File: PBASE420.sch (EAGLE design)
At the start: 13 parts, among them J1 DC_2_1MM, SW1 MK-12C02-PB

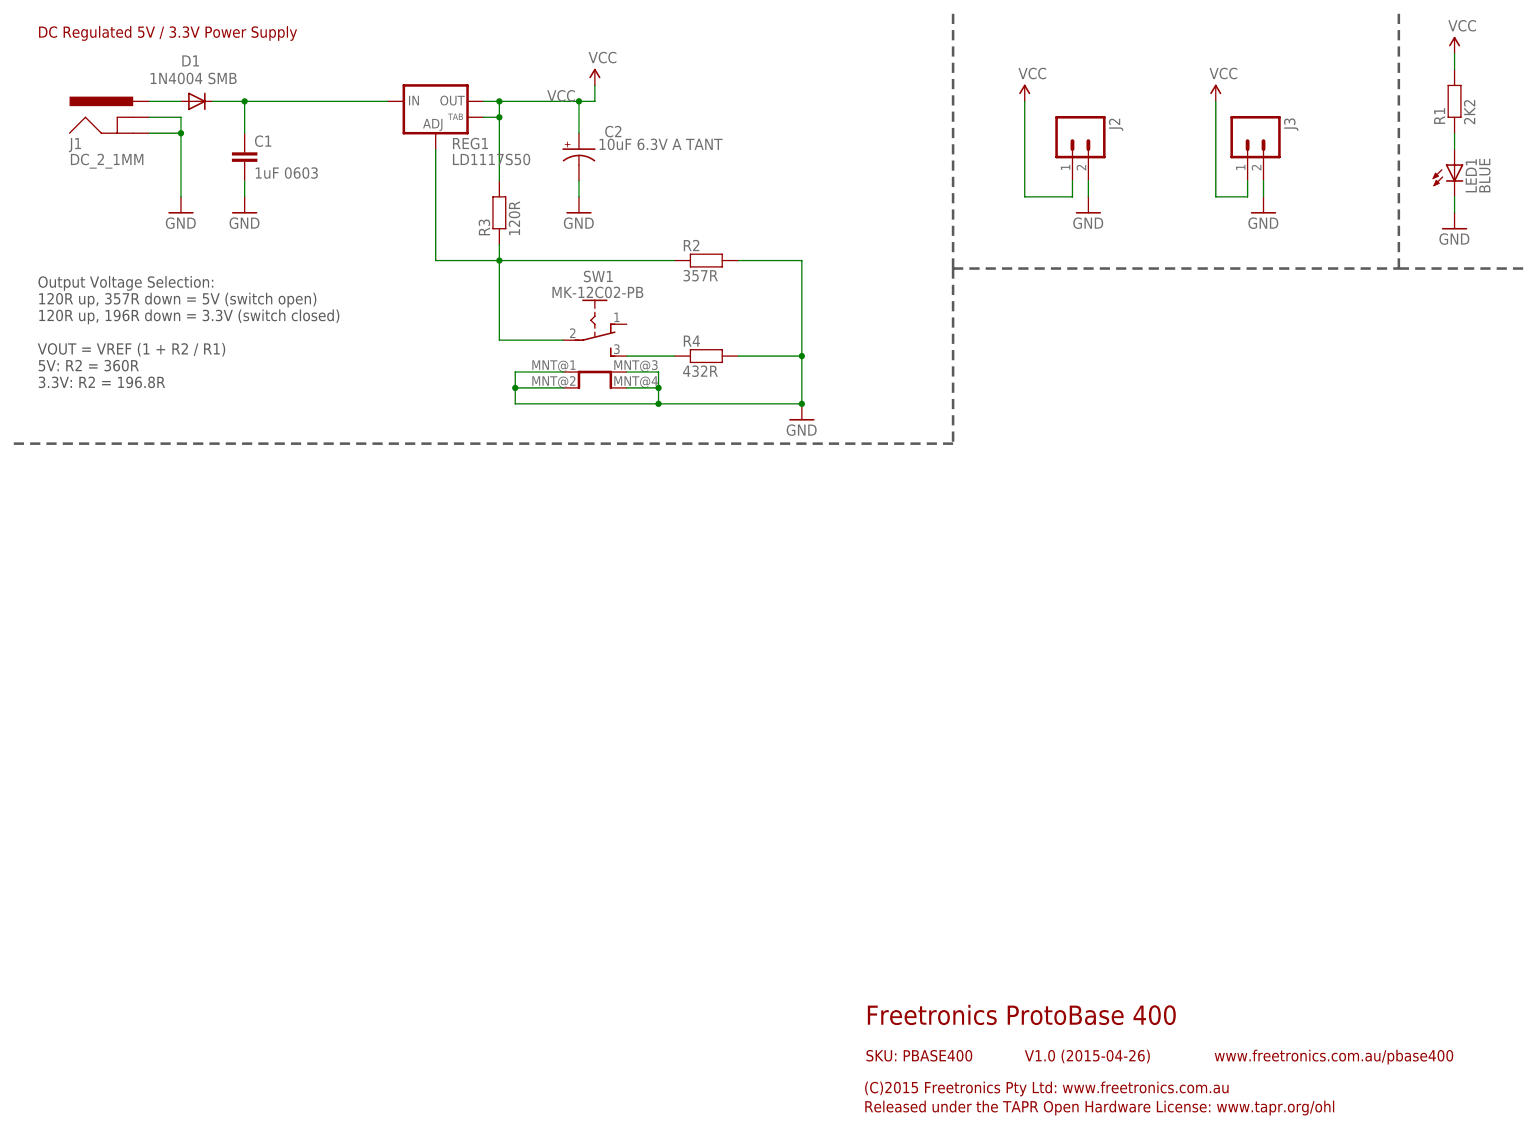
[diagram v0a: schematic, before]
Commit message: Updated silkscreen, designators, and README
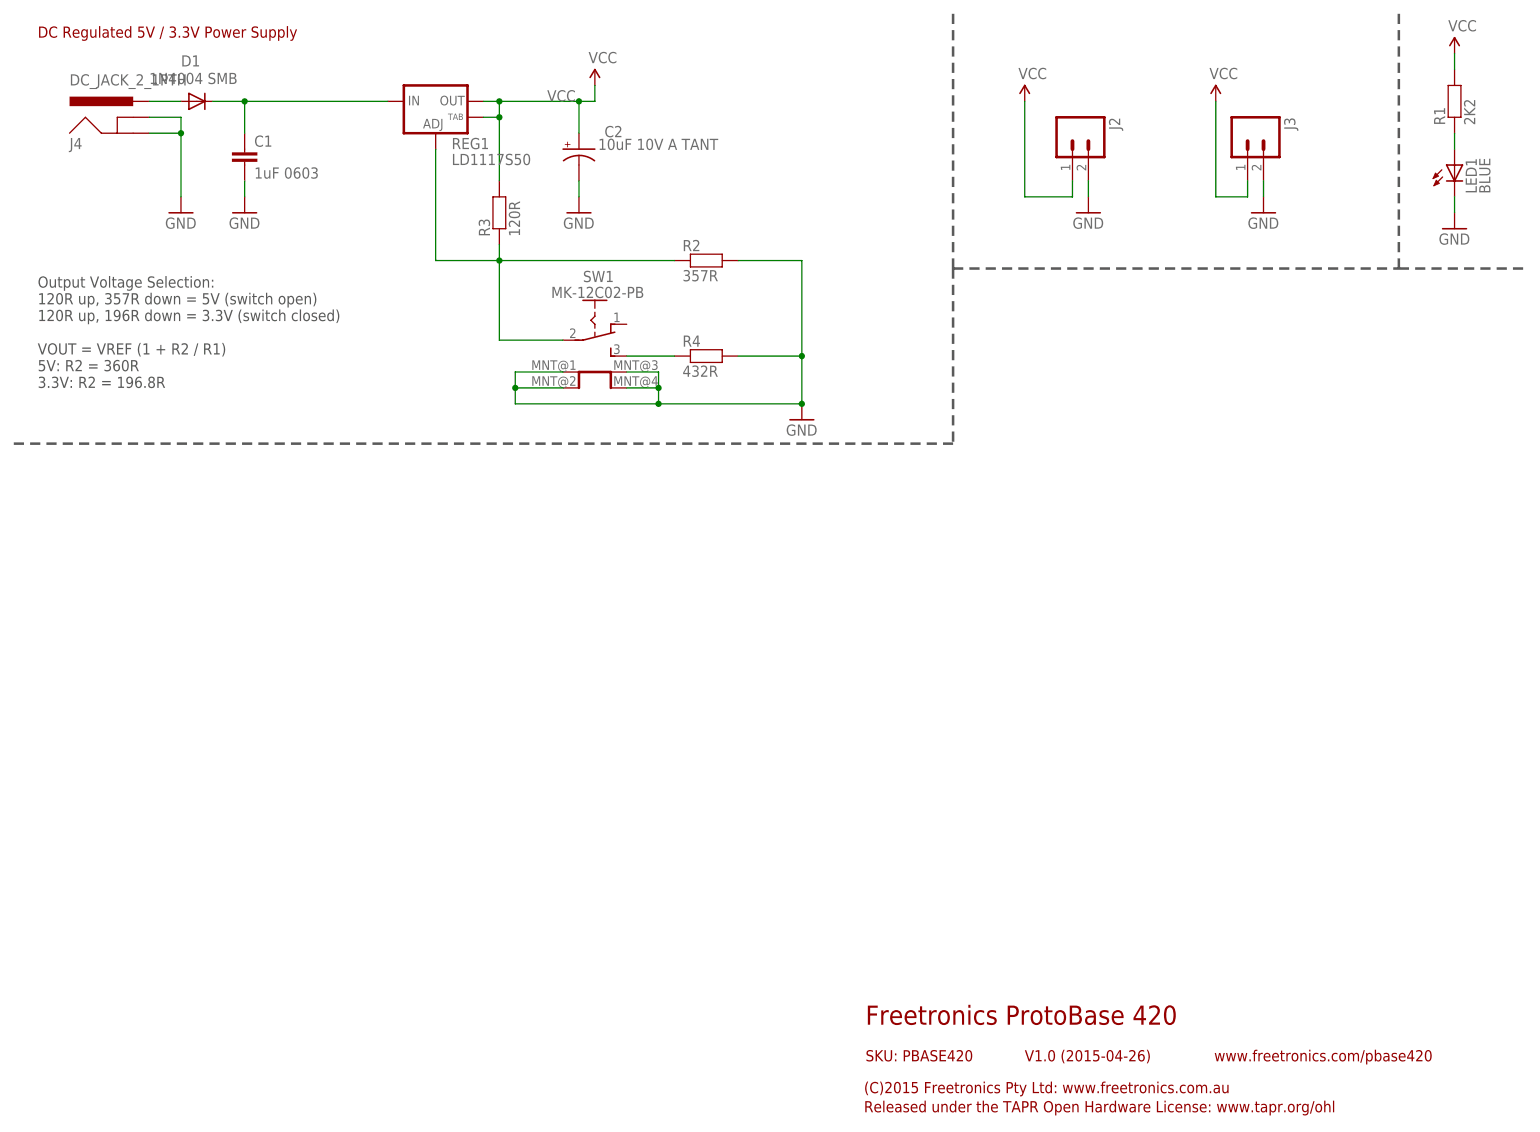
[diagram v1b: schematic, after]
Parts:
- removed J1: DC_2_1MM, freetronics:POWER_JACKPTH
- added J4: DC_JACK_2_1PTH, DCJackSlots:DC_JACK_2_1PTH
- C2: value 10uF 6.3V A TANT -> 10uF 10V A TANT
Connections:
- net GND: now also J4.GND, J4.GNDBREAK; no longer J1.GND, J1.GNDBREAK
- net N$8: now also J4.PWR; no longer J1.PWR
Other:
- note added: "Freetronics ProtoBase 420"
- note added: "SKU: PBASE420"
- note added: "www.freetronics.com/pbase420"
- note removed: "Freetronics ProtoBase 400"
- note removed: "SKU: PBASE400"
- note removed: "www.freetronics.com.au/pbase400"
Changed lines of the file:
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@@
 </classes>
 <parts>
-<part name="J1" library="freetronics" deviceset="POWER_JACK" device="PTH" value="DC_2_1MM"/>
 <part name="D1" library="freetronics" deviceset="DIODE" device="SMB" value="1N4004 SMB"/>
 <part name="GND12" library="SparkFun" deviceset="GND" device=""/>
@@
 <part name="R4" library="freetronics-jon" deviceset="RESISTOR" device="0603" value="432R"/>
 <part name="GND4" library="SparkFun" deviceset="GND" device=""/>
-<part name="C2" library="freetronics" deviceset="CAP_POL" device="1206" value="10uF 6.3V A TANT"/>
+<part name="C2" library="freetronics" deviceset="CAP_POL" device="1206" value="10uF 10V A TANT"/>
+<part name="J4" library="DCJackSlots" deviceset="DC_JACK_2_1" device="PTH"/>
 </parts>
 <sheets>
@@
 <text x="7.62" y="177.8" size="1.778" layer="94">DC Regulated 5V / 3.3V Power Supply</text>
 <frame x1="0" y1="0" x2="248.92" y2="185.42" columns="8" rows="5" layer="94"/>
-<text x="139.7" y="20.32" size="3.048" layer="94">Freetronics ProtoBase 400</text>
+<text x="139.7" y="20.32" size="3.048" layer="94">Freetronics ProtoBase 420</text>
 <text x="165.1" y="14.478" size="1.778" layer="94">V1.0 (2015-04-26)</text>
-<text x="139.7" y="14.478" size="1.778" layer="94">SKU: PBASE400</text>
+<text x="139.7" y="14.478" size="1.778" layer="94">SKU: PBASE420</text>
 <text x="139.446" y="9.398" size="1.778" layer="94">(C)2015 Freetronics Pty Ltd: www.freetronics.com.au</text>
 <text x="139.446" y="6.35" size="1.778" layer="94">Released under the TAPR Open Hardware License: www.tapr.org/ohl</text>
-<text x="195.326" y="14.478" size="1.778" layer="94">www.freetronics.com.au/pbase400</text>
+<text x="195.326" y="14.478" size="1.778" layer="94">www.freetronics.com/pbase420</text>
 <frame x1="137.16" y1="12.7" x2="243.84" y2="25.4" columns="0" rows="0" layer="94" border-left="no" border-top="no" border-right="no" border-bottom="no"/>
 <frame x1="162.56" y1="12.7" x2="193.04" y2="17.78" columns="8" rows="5" layer="94"/>
@@
 </plain>
 <instances>
-<instance part="J1" gate="G$1" x="22.86" y="160.02" smashed="yes">
-<attribute name="NAME" x="12.7" y="160.02" size="1.778" layer="95"/>
-<attribute name="VALUE" x="12.7" y="157.48" size="1.778" layer="96"/>
-</instance>
 <instance part="D1" gate="G$1" x="33.02" y="167.64" smashed="yes">
 <attribute name="NAME" x="30.48" y="173.2026" size="1.778" layer="95"/>
@@
 <attribute name="VALUE" x="97.028" y="159.893" size="1.778" layer="96"/>
 </instance>
+<instance part="J4" gate="G$1" x="22.86" y="160.02"/>
 </instances>
 <busses>
@@
 <junction x="30.48" y="162.56"/>
 <pinref part="GND12" gate="1" pin="GND"/>
-<pinref part="J1" gate="G$1" pin="GNDBREAK"/>
-<pinref part="J1" gate="G$1" pin="GND"/>
+<pinref part="J4" gate="G$1" pin="GND"/>
+<pinref part="J4" gate="G$1" pin="GNDBREAK"/>
 </segment>
 <segment>
@@
 <segment>
 <wire x1="25.4" y1="167.64" x2="30.48" y2="167.64" width="0.1524" layer="91"/>
-<pinref part="J1" gate="G$1" pin="PWR"/>
 <pinref part="D1" gate="G$1" pin="A"/>
+<pinref part="J4" gate="G$1" pin="PWR"/>
 </segment>
 </net>

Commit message: Replaced DC jack footprint with slotted version
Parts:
- J4: value DC_JACK_2_1PTH -> POWER_JACKPTH_SLOTS; device DCJackSlots:DC_JACK_2_1PTH -> freetronics-jon:POWER_JACKPTH_SLOTS
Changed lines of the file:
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@@
 <?xml version="1.0" encoding="utf-8"?>
 <!DOCTYPE eagle SYSTEM "eagle.dtd">
-<eagle version="6.5.0">
+<eagle version="8.7.0">
 <drawing>
 <settings>
-<setting alwaysvectorfont="yes"/>
+<setting alwaysvectorfont="no"/>
+<setting keepoldvectorfont="yes"/>
 <setting verticaltext="up"/>
 </settings>
@@
 <layer number="54" name="bGND_GNDA" color="1" fill="9" visible="no" active="no"/>
 <layer number="56" name="wert" color="7" fill="1" visible="no" active="no"/>
+<layer number="57" name="tCAD" color="7" fill="1" visible="no" active="no"/>
+<layer number="59" name="tCarbon" color="7" fill="1" visible="no" active="no"/>
 <layer number="60" name="p_dimension" color="6" fill="0" visible="no" active="no"/>
 <layer number="61" name="pt_docu" color="7" fill="0" visible="no" active="no"/>
+<layer number="88" name="SimResults" color="9" fill="1" visible="yes" active="yes"/>
+<layer number="89" name="SimProbes" color="9" fill="1" visible="yes" active="yes"/>
+<layer number="90" name="Modules" color="7" fill="1" visible="yes" active="yes"/>
 <layer number="91" name="Nets" color="2" fill="1" visible="yes" active="yes"/>
 <layer number="92" name="Busses" color="1" fill="1" visible="yes" active="yes"/>
@@
 <layer number="97" name="Info" color="7" fill="1" visible="yes" active="yes"/>
 <layer number="98" name="Guide" color="6" fill="1" visible="yes" active="yes"/>
+<layer number="99" name="SpiceOrder" color="7" fill="1" visible="no" active="no"/>
 <layer number="100" name="Muster" color="7" fill="1" visible="no" active="no"/>
 <layer number="101" name="Patch_Top" color="12" fill="4" visible="yes" active="yes"/>
@@
 <layer number="111" name="LPC17xx" color="7" fill="1" visible="yes" active="yes"/>
 <layer number="112" name="tSilk" color="7" fill="1" visible="yes" active="yes"/>
+<layer number="113" name="ReferenceLS" color="7" fill="1" visible="no" active="no"/>
 <layer number="116" name="Patch_BOT" color="9" fill="4" visible="yes" active="yes"/>
 <layer number="118" name="Rect_Pads" color="7" fill="1" visible="yes" active="yes"/>
@@
 <layer number="127" name="_tValues" color="7" fill="1" visible="yes" active="yes"/>
 <layer number="128" name="_bValues" color="7" fill="1" visible="yes" active="yes"/>
+<layer number="129" name="Mask" color="7" fill="1" visible="yes" active="yes"/>
 <layer number="131" name="tAdjust" color="7" fill="1" visible="yes" active="yes"/>
 <layer number="132" name="bAdjust" color="7" fill="1" visible="yes" active="yes"/>
@@
 <layer number="146" name="p_Milling" color="3" fill="9" visible="yes" active="yes"/>
 <layer number="147" name="COVER" color="14" fill="1" visible="yes" active="yes"/>
+<layer number="150" name="Notes" color="7" fill="1" visible="yes" active="yes"/>
 <layer number="151" name="HeatSink" color="7" fill="1" visible="yes" active="yes"/>
 <layer number="152" name="_bDocu" color="7" fill="1" visible="yes" active="yes"/>
+<layer number="153" name="FabDoc1" color="6" fill="1" visible="no" active="no"/>
+<layer number="154" name="FabDoc2" color="2" fill="1" visible="no" active="no"/>
+<layer number="155" name="FabDoc3" color="7" fill="15" visible="no" active="no"/>
 <layer number="190" name="Comments" color="12" fill="1" visible="yes" active="yes"/>
 <layer number="199" name="Contour" color="7" fill="1" visible="yes" active="yes"/>
@@
 <layer number="223" name="223bmp" color="7" fill="1" visible="yes" active="yes"/>
 <layer number="224" name="224bmp" color="7" fill="1" visible="yes" active="yes"/>
+<layer number="225" name="225bmp" color="7" fill="1" visible="yes" active="yes"/>
+<layer number="226" name="226bmp" color="7" fill="1" visible="yes" active="yes"/>
+<layer number="227" name="227bmp" color="7" fill="1" visible="yes" active="yes"/>
+<layer number="228" name="228bmp" color="7" fill="1" visible="yes" active="yes"/>
+<layer number="229" name="229bmp" color="7" fill="1" visible="yes" active="yes"/>
+<layer number="230" name="230bmp" color="7" fill="1" visible="yes" active="yes"/>
 <layer number="231" name="Eagle3D_PG1" color="7" fill="1" visible="yes" active="yes"/>
 <layer number="232" name="Eagle3D_PG2" color="7" fill="1" visible="yes" active="yes"/>
@@
 <layer number="251" name="SMDround" color="12" fill="11" visible="no" active="no"/>
 <layer number="254" name="cooling" color="7" fill="1" visible="yes" active="yes"/>
+<layer number="255" name="routoute" color="7" fill="1" visible="yes" active="yes"/>
 </layers>
 <schematic xreflabel="%F%N/%S.%C%R" xrefpart="/%S.%C%R">
@@
 <part name="GND4" library="SparkFun" deviceset="GND" device=""/>
 <part name="C2" library="freetronics" deviceset="CAP_POL" device="1206" value="10uF 10V A TANT"/>
-<part name="J4" library="DCJackSlots" deviceset="DC_JACK_2_1" device="PTH"/>
+<part name="J4" library="freetronics-jon" deviceset="POWER_JACK" device="PTH_SLOTS"/>
 </parts>
 <sheets>
@@
 <attribute name="VALUE" x="97.028" y="159.893" size="1.778" layer="96"/>
 </instance>
-<instance part="J4" gate="G$1" x="22.86" y="160.02"/>
+<instance part="J4" gate="G$1" x="22.86" y="160.02" smashed="yes">
+<attribute name="NAME" x="12.7" y="160.02" size="1.778" layer="95"/>
+</instance>
 </instances>
 <busses>
